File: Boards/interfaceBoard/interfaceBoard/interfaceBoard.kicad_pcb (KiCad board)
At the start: 2 copper layers, 100 x 100 mm, 49 parts, among them J1 Interface With Arduino, J2 12V input (molex), J3 Barrel_Jack_Switch, J4 MISO interface connector (Rea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, J5 Conn_02x09_Odd_Even, J6 DaisyCainOut, U1 74HC595, U2 TBD62783A, U3 74HC165, U4 74HC595, U5 TBD62783A, U6 74HC165

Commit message: Big progress
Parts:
- removed R10, R12, R14, R16, R18, R20, R22, R24, R26, R28, R30, R32, R34, R4, R6, R8: 100K, Resistor_THT:R_Axial_DIN0207_L6.3mm_D2.5mm_P10.16mm_Horizontal
- removed R11, R13, R15, R17, R19, R21, R23, R25, R27, R29, R31, R33, R5, R7, R9: 200K, Resistor_THT:R_Axial_DIN0207_L6.3mm_D2.5mm_P10.16mm_Horizontal
- added D3: LED, LED_THT:LED_D3.0mm, F.Cu at (68.4, 72.0)
- added RN1: R_Pack08, Package_DIP:DIP-16_W7.62mm_Socket, F.Cu at (90.0, 104.8)
- added RN2: R_Network08, Resistor_THT:R_Array_SIP9, F.Cu at (85.5, 102.3)
- added RN3: R_Pack08, Package_DIP:DIP-16_W7.62mm_Socket, F.Cu at (123.0, 105.4)
- added RN4: R_Network08, Resistor_THT:R_Array_SIP9, F.Cu at (118.5, 102.9)
- added RN5: R_Pack08, Package_DIP:DIP-16_W7.62mm_Socket, F.Cu at (91.1, 129.8)
- added RN6: R_Network08, Resistor_THT:R_Array_SIP9, F.Cu at (86.6, 127.2)
- added RN7: R_Pack08, Package_DIP:DIP-16_W7.62mm_Socket, F.Cu at (124.4, 130.1)
- added RN8: R_Network08, Resistor_THT:R_Array_SIP9, F.Cu at (119.9, 127.6)
- added SW1: SW_SPDT, myLibrary:SW_SPDT_SS-12D10L5, F.Cu at (71.5, 87.5)
- added U12: 74HC165, Package_DIP:DIP-16_W7.62mm_Socket, F.Cu at (104.4, 130.1)
- added U4: 74HC165, Package_DIP:DIP-16_W7.62mm_Socket, F.Cu at (103.0, 105.4)
- added U5: 74HC165, Package_DIP:DIP-16_W7.62mm_Socket, F.Cu at (71.1, 129.8)
- added U7: TBD62783A, Package_DIP:DIP-18_W7.62mm_Socket, F.Cu at (87.5, 76.9)
- added U8: 74HC595, Package_DIP:DIP-16_W7.62mm_Socket, F.Cu at (127.7, 76.8)
- added U9: TBD62783A, Package_DIP:DIP-18_W7.62mm_Socket, F.Cu at (116.0, 76.8)
- J4: value MISO interface connector (Read) -> Conn_02x17_Odd_Even; footprint Connector_PinHeader_2.54mm:PinHeader_2x09_P2.54mm_Vertical -> Connector_PinHeader_2.54mm:PinHeader_2x17_P2.54mm_Vertical
- J5: value Conn_02x09_Odd_Even -> Conn_02x17_Odd_Even; footprint Connector_PinHeader_2.54mm:PinHeader_2x09_P2.54mm_Vertical -> Connector_PinHeader_2.54mm:PinHeader_2x17_P2.54mm_Vertical
- R3: value 200K -> R
- U6: value 74HC165 -> 74HC595
- moved J4 67.4 mm to (145.0, 52.3)
- moved R3 59.9 mm to (82.1, 73.0)
- moved J5 51.5 mm to (145.0, 105.3)
- moved U6 44.8 mm to (99.2, 76.9)
- moved U3 24.2 mm to (70.0, 104.9)
- moved D2 14.5 mm to (68.4, 65.1)
- moved D1 14.4 mm to (68.4, 59.7)
- moved R2 13.0 mm to (82.1, 61.0)
- moved R1 12.9 mm to (82.1, 66.2)
- moved F1 10.2 mm to (77.5, 87.5), turned to 90 degrees
- moved U2 2.50 mm to (99.0, 51.9)
- moved J3 1.58 mm to (52.4, 55.0)
- moved U11 1.50 mm to (127.9, 51.8)
- moved J6 0.79 mm to (52.5, 148.0)
- renumbered J2 to J1, J3 to J2, J1 to J3, U4 to U10, U5 to U11
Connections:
- F1 pad 1: Net-(J2-Pin_2) -> Net-(SW1-B)
- J1 pad 2: Net-(J2-Pin_2) -> Net-(J1-Pin_2)
- J2 pad 1: Net-(J2-Pin_2) -> Net-(SW1-A)
- J4 pad 10: /MISO_sheet1/D0 -> /MOSI_sheet1/O1
- J4 pad 11: /MISO_sheet1/D1 -> /MOSI_sheet1/O2
- J4 pad 12: /MISO_sheet1/D2 -> /MOSI_sheet1/O3
- J4 pad 13: /MISO_sheet1/D3 -> /MOSI_sheet1/O4
- J4 pad 14: /MISO_sheet1/D4 -> /MOSI_sheet1/O5
- J4 pad 15: /MISO_sheet1/D5 -> /MOSI_sheet1/O6
- J4 pad 16: /MISO_sheet1/D6 -> /MOSI_sheet1/O7
- J4 pad 17: /MISO_sheet1/D7 -> /MOSI_sheet1/O8
- J4 pad 18: GND -> /MOSI_sheet2/O1
- J4 pad 2: /MISO_sheet/D0 -> /MOSI_sheet/O1
- J4 pad 3: /MISO_sheet/D1 -> /MOSI_sheet/O2
- J4 pad 4: /MISO_sheet/D2 -> /MOSI_sheet/O3
- J4 pad 5: /MISO_sheet/D3 -> /MOSI_sheet/O4
- J4 pad 6: /MISO_sheet/D4 -> /MOSI_sheet/O5
- J4 pad 7: /MISO_sheet/D5 -> /MOSI_sheet/O6
- J4 pad 8: /MISO_sheet/D6 -> /MOSI_sheet/O7
- J4 pad 9: /MISO_sheet/D7 -> /MOSI_sheet/O8
- J5 pad 10: /MOSI_sheet1/O1 -> /MISO_sheet1/D0
- J5 pad 11: /MOSI_sheet1/O2 -> /MISO_sheet1/D1
- J5 pad 12: /MOSI_sheet1/O3 -> /MISO_sheet1/D2
- J5 pad 13: /MOSI_sheet1/O4 -> /MISO_sheet1/D3
- J5 pad 14: /MOSI_sheet1/O5 -> /MISO_sheet1/D4
- J5 pad 15: /MOSI_sheet1/O6 -> /MISO_sheet1/D5
- J5 pad 16: /MOSI_sheet1/O7 -> /MISO_sheet1/D6
- J5 pad 17: /MOSI_sheet1/O8 -> /MISO_sheet1/D7
- J5 pad 18: GND -> /MISO_sheet2/D0
- J5 pad 2: /MOSI_sheet/O1 -> /MISO_sheet/D0
- J5 pad 3: /MOSI_sheet/O2 -> /MISO_sheet/D1
- J5 pad 4: /MOSI_sheet/O3 -> /MISO_sheet/D2
- J5 pad 5: /MOSI_sheet/O4 -> /MISO_sheet/D3
- J5 pad 6: /MOSI_sheet/O5 -> /MISO_sheet/D4
- J5 pad 7: /MOSI_sheet/O6 -> /MISO_sheet/D5
- J5 pad 8: /MOSI_sheet/O7 -> /MISO_sheet/D6
- J5 pad 9: /MOSI_sheet/O8 -> /MISO_sheet/D7
- J6 pad 3: /MOSI_sheet1/QH' -> /MOSI_sheet3/QH'
- J6 pad 4: /MISO_sheet1/SerIn -> /MISO_sheet3/SerIn
- R3 pad 1: /MISO_sheet/D1 -> 12V+
- R3 pad 2: /MISO_sheet/vDiv1/OUT -> Net-(D3-A)
- U3 pad 11: /MISO_sheet/vDiv0/OUT -> Net-(RN1-R8.1)
- U3 pad 12: /MISO_sheet/vDiv1/OUT -> Net-(RN1-R7.1)
- U3 pad 13: /MISO_sheet/vDiv2/OUT -> Net-(RN1-R6.1)
- U3 pad 14: /MISO_sheet/vDiv3/OUT -> Net-(RN1-R5.1)
- U3 pad 16: /MISO_sheet/5V+ -> 5V+
- U3 pad 3: /MISO_sheet/vDiv4/OUT -> Net-(RN1-R4.1)
- U3 pad 4: /MISO_sheet/vDiv5/OUT -> Net-(RN1-R3.1)
- U3 pad 5: /MISO_sheet/vDiv6/OUT -> Net-(RN1-R2.1)
- U3 pad 6: /MISO_sheet/vDiv7/OUT -> Net-(RN1-R1.1)
- U3 pad 9: /MISO_sheet/Q7 -> /MISO
- U6 pad 1: LOAD -> /MOSI_sheet2/QB
- U6 pad 10: /MISO_sheet1/SerIn -> 5V+
- U6 pad 11: /MISO_sheet1/vDiv0/OUT -> CLK
- U6 pad 12: /MISO_sheet1/vDiv1/OUT -> LATCH
- U6 pad 13: /MISO_sheet1/vDiv2/OUT -> GND
- U6 pad 14: /MISO_sheet1/vDiv3/OUT -> /MOSI_sheet1/QH'
- U6 pad 15: GND -> /MOSI_sheet2/QA
- U6 pad 16: /MISO_sheet1/5V+ -> 5V+
- U6 pad 2: CLK -> /MOSI_sheet2/QC
- U6 pad 3: /MISO_sheet1/vDiv4/OUT -> /MOSI_sheet2/QD
- U6 pad 4: /MISO_sheet1/vDiv5/OUT -> /MOSI_sheet2/QE
- U6 pad 5: /MISO_sheet1/vDiv6/OUT -> /MOSI_sheet2/QF
- U6 pad 6: /MISO_sheet1/vDiv7/OUT -> /MOSI_sheet2/QG
- U6 pad 7: unconnected-(U6-~{Q7}-Pad7) -> /MOSI_sheet2/QH
- U6 pad 9: /MISO_sheet/SerIn -> /MOSI_sheet2/QH'
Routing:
- net Net-(RN5-R1.1): track 0.00 -> 32.2 mm
- net Net-(RN3-R1.1): track 0.00 -> 32.2 mm
- net Net-(RN7-R1.1): track 0.00 -> 32.2 mm
- net Net-(RN1-R1.1): track 0.00 -> 32.2 mm
- net /MISO_sheet/vDiv3/OUT: track 26.5 -> 0.00 mm
- net /MISO_sheet1/vDiv3/OUT: track 26.5 -> 0.00 mm
- net /MISO_sheet/vDiv0/OUT: track 26.5 -> 0.00 mm
- net /MISO_sheet1/vDiv0/OUT: track 26.5 -> 0.00 mm
- net Net-(RN5-R4.1): track 0.00 -> 25.4 mm
- net Net-(RN1-R4.1): track 0.00 -> 25.4 mm
- net Net-(RN3-R4.1): track 0.00 -> 25.4 mm
- net Net-(RN7-R4.1): track 0.00 -> 25.4 mm
- net /MISO_sheet/vDiv1/OUT: track 24.4 -> 0.00 mm
- net /MISO_sheet1/vDiv1/OUT: track 24.4 -> 0.00 mm
- net /MISO_sheet/vDiv2/OUT: track 24.4 -> 0.00 mm
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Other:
- board text added: "ARDUINO STATUS LEDs"
- board text added: "BLUE: 12V+ POWER STATUS"
- board text added: "RED: STANDBY REG&GREEN: RUNNING GREEN: DONE SUCCESS! GREEN&RED BLINK: DONE FAIL"

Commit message: BEFORE FUCKING EVERYTHING UP
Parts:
- moved U8 19.4 mm to (123.2, 95.7), turned to 180 degrees
- moved U6 19.3 mm to (94.7, 95.7), turned to 180 degrees
- moved U9 12.1 mm to (128.1, 76.9)
- moved U7 12.1 mm to (99.6, 76.9)
- moved J3 7.55 mm to (59.8, 53.5), turned to -90 degrees
- moved RN4 1.73 mm to (119.8, 101.7)
- moved U4 1.73 mm to (104.3, 104.3)
- moved RN3 1.73 mm to (124.3, 104.3)
- moved U5 1.12 mm to (70.0, 130.1)
- moved RN5 1.12 mm to (90.0, 130.1)
- moved RN6 1.12 mm to (85.5, 127.6)
- moved U10 1.04 mm to (123.2, 70.5)
- moved U2 0.62 mm to (99.6, 51.8)
- moved U1 0.62 mm to (94.7, 70.5)
- moved RN1 0.58 mm to (90.0, 104.3)
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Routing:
- net 12V+: track 0.00 -> 118.7 mm
- net 5V+: track 0.00 -> 64.7 mm
- net /STATUS: track 0.00 -> 41.5 mm
- net Net-(D2-A): track 0.00 -> 16.7 mm
- net /MOSI_sheet2/QA: track 0.00 -> 14.9 mm
- net /MOSI_sheet1/QA: track 0.00 -> 14.9 mm
- net /MOSI_sheet/QA: track 0.00 -> 14.9 mm
- net /MOSI_sheet3/QA: track 0.00 -> 14.9 mm
- net /MOSI_sheet2/QG: track 0.00 -> 6.35 mm
- net /MOSI_sheet2/QF: track 0.00 -> 6.35 mm
- net /MOSI_sheet2/QD: track 0.00 -> 6.35 mm
- net /MOSI_sheet2/QB: track 0.00 -> 6.35 mm
- net /MOSI_sheet3/QH: track 0.00 -> 6.35 mm
- net /MOSI_sheet3/QF: track 0.00 -> 6.35 mm
- net /MOSI_sheet3/QD: track 0.00 -> 6.35 mm
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
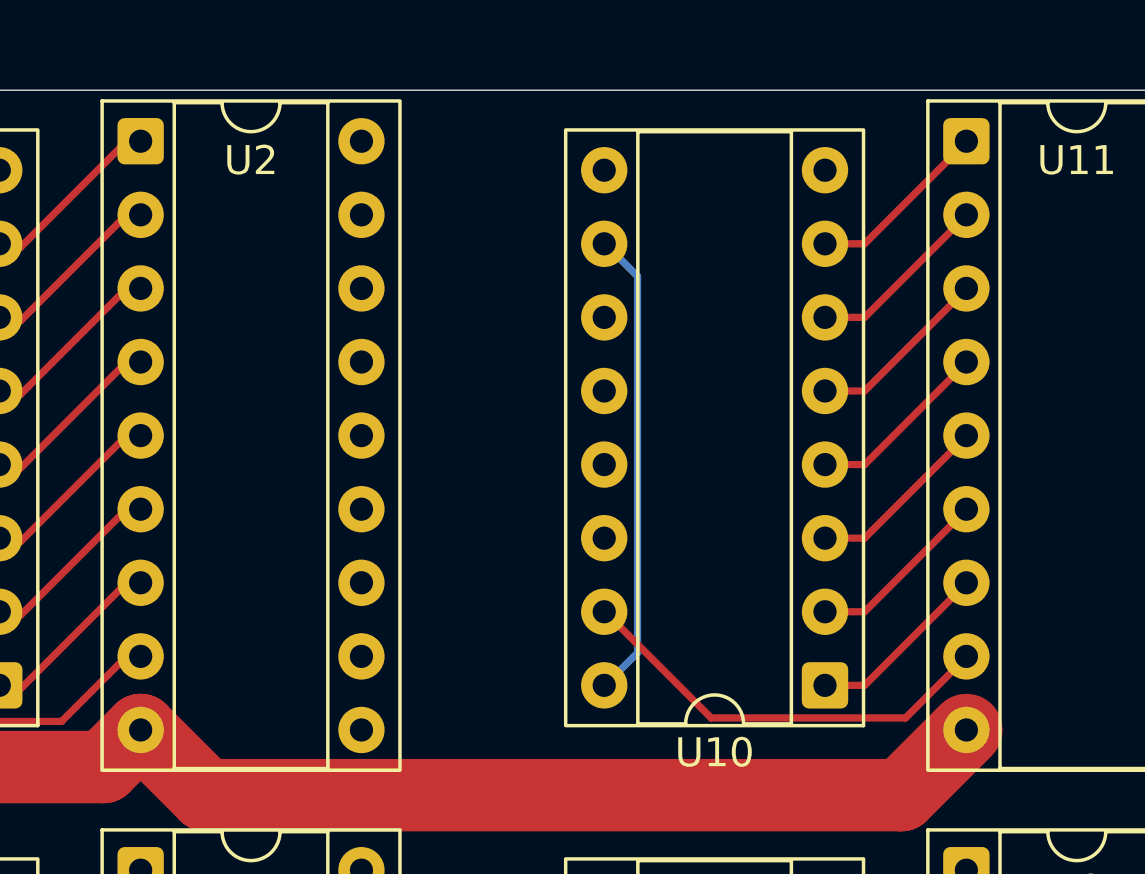
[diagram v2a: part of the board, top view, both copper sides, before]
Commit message: Update interfaceBoard.kicad_pcb
Started routing MOSI
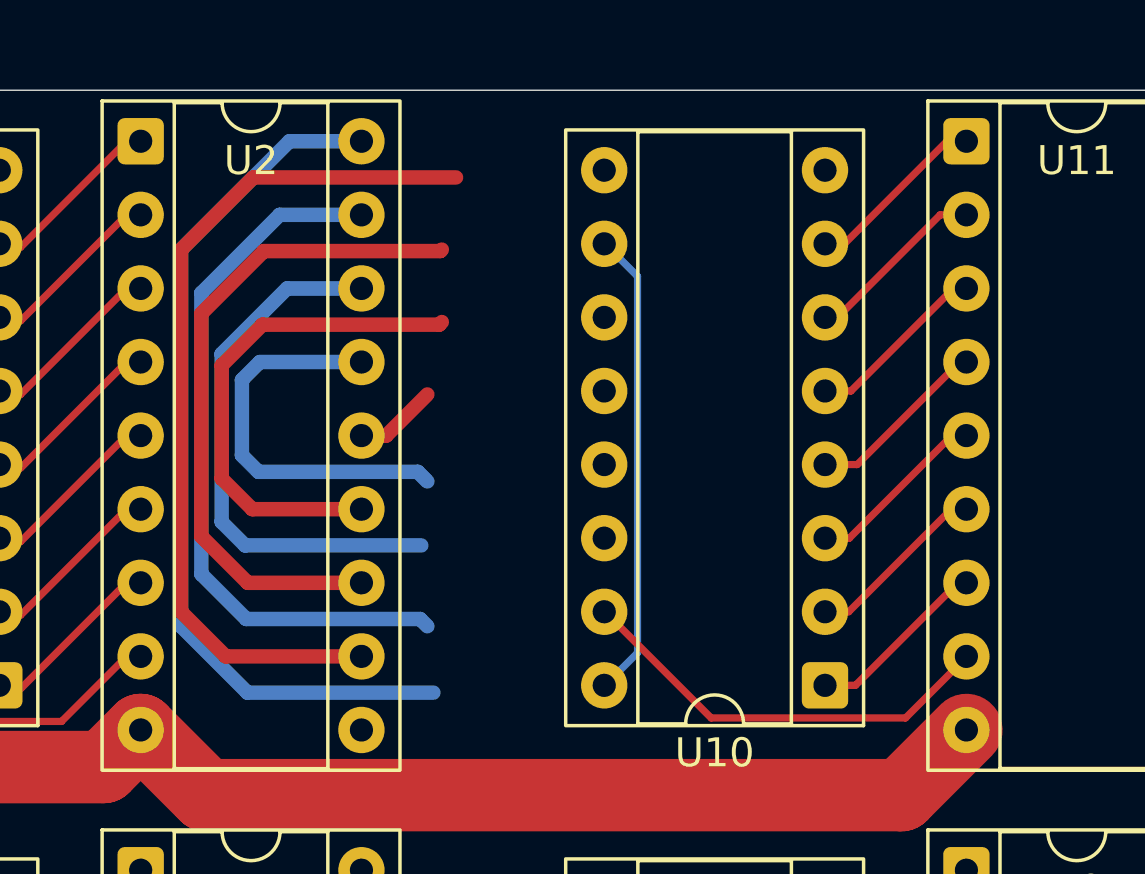
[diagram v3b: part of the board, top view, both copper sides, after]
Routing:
- net /MOSI_sheet/O8: track 0.00 -> 30.4 mm
- net /MOSI_sheet/O1: track 0.00 -> 29.9 mm
- net /MOSI_sheet/O7: track 0.00 -> 24.9 mm
- net /MOSI_sheet/O2: track 0.00 -> 23.1 mm
- net /MOSI_sheet/O6: track 0.00 -> 18.8 mm
- net /MOSI_sheet/O3: track 0.00 -> 17.4 mm
- net /MOSI_sheet/O5: track 0.00 -> 13.8 mm
- net /MOSI_sheet/O4: track 0.00 -> 2.86 mm

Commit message: Update interfaceBoard.kicad_pcb
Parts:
- moved J4 75.5 mm to (210.3, 90.3), turned to 180 degrees
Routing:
- net /MOSI_sheet/O8: track 30.4 -> 0.00 mm
- net /MOSI_sheet/O1: track 29.9 -> 0.00 mm
- net /MOSI_sheet/O7: track 24.9 -> 0.00 mm
- net /MOSI_sheet/O2: track 23.1 -> 0.00 mm
- net /MOSI_sheet/O6: track 18.8 -> 0.00 mm
- net /MOSI_sheet/O3: track 17.4 -> 0.00 mm
- net /MOSI_sheet/O5: track 13.8 -> 0.00 mm
- net /MOSI_sheet/O4: track 2.86 -> 0.00 mm

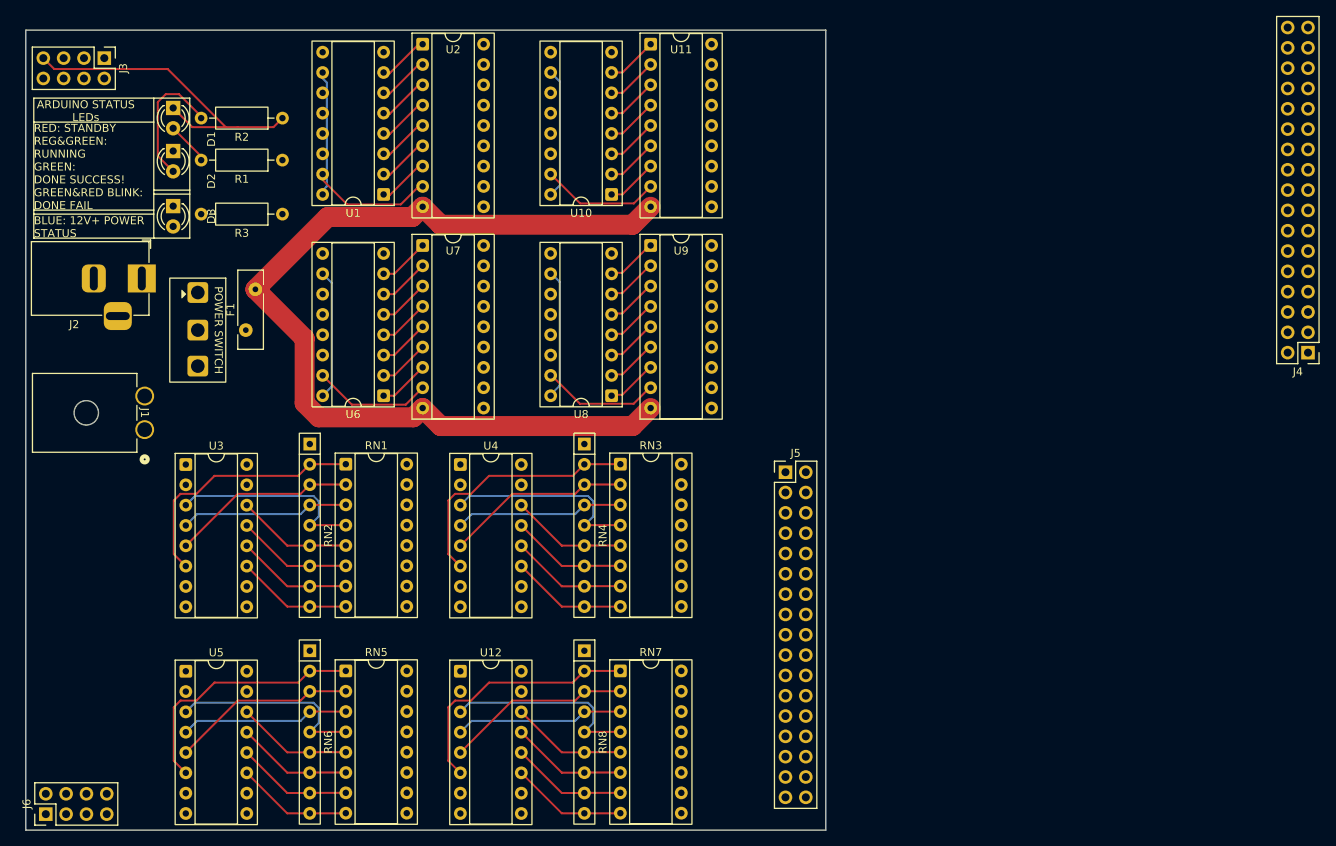
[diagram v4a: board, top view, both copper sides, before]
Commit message: WIP MOSI
Rearanged MOSI channels and wires MOSI0 and MOSI1 to output connector
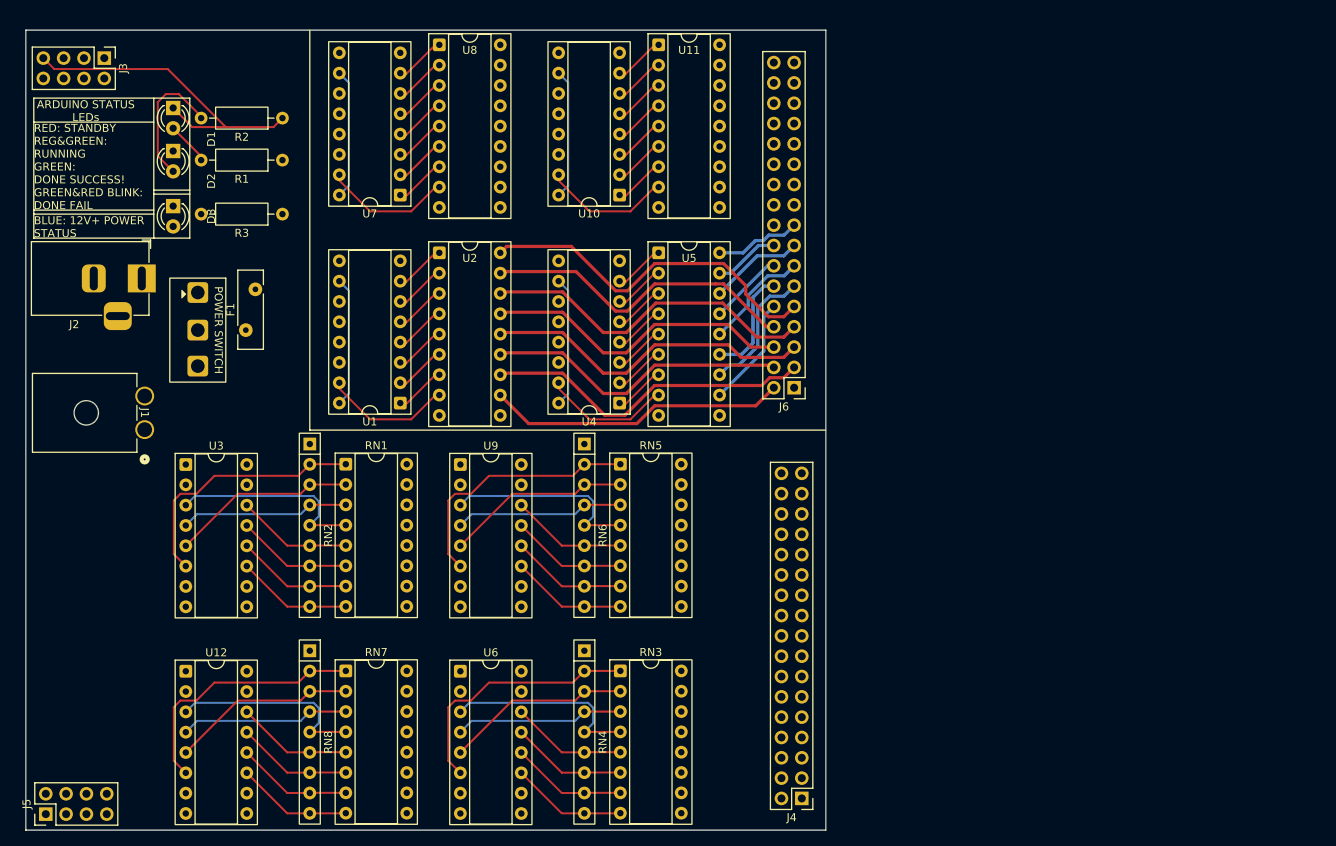
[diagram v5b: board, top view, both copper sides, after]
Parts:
- moved J6 64.4 mm to (146.0, 94.7)
- moved J4 40.8 mm to (147.0, 146.0), turned to 180 degrees
- moved U2 26.2 mm to (101.7, 77.8)
- moved U1 26.2 mm to (96.8, 96.6)
- moved U5 26.1 mm to (129.1, 77.8)
- moved U4 26.1 mm to (124.2, 96.6)
- moved U7 25.2 mm to (96.8, 70.6)
- moved U8 25.2 mm to (101.7, 51.8)
- moved U10 25.1 mm to (124.2, 70.6)
- moved U11 25.1 mm to (129.1, 51.8)
- renumbered J5 to J4, J6 to J5, J4 to J6, RN7 to RN3, RN8 to RN4, RN3 to RN5, RN4 to RN6, RN5 to RN7, RN6 to RN8, U8 to U10, U9 to U11, U5 to U12, U10 to U4, U11 to U5, U12 to U6, U6 to U7, U7 to U8, U4 to U9
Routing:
- net 12V+: track 118.7 -> 0.00 mm
- net /MOSI_sheet/O8: track 0.00 -> 44.7 mm
- net /MOSI_sheet/O6: track 0.00 -> 42.7 mm
- net /MOSI_sheet/O4: track 0.00 -> 41.6 mm
- net /MOSI_sheet/O2: track 0.00 -> 41.5 mm
- net /MOSI_sheet/O7: track 0.00 -> 39.9 mm
- net /MOSI_sheet/O5: track 0.00 -> 39.0 mm
- net /MOSI_sheet/O3: track 0.00 -> 38.0 mm
- net /MOSI_sheet/O1: track 0.00 -> 37.5 mm
- net /MOSI_sheet1/O2: track 0.00 -> 16.7 mm
- net /MOSI_sheet1/O1: track 0.00 -> 13.9 mm
- net /MOSI_sheet1/O3: track 0.00 -> 13.7 mm
- net /MOSI_sheet1/O4: track 0.00 -> 13.6 mm
- net /MOSI_sheet1/O6: track 0.00 -> 11.8 mm
- net /MOSI_sheet1/O8: track 0.00 -> 10.7 mm
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
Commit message: MOSI done?
MOSI wired.
MISO wired to interface
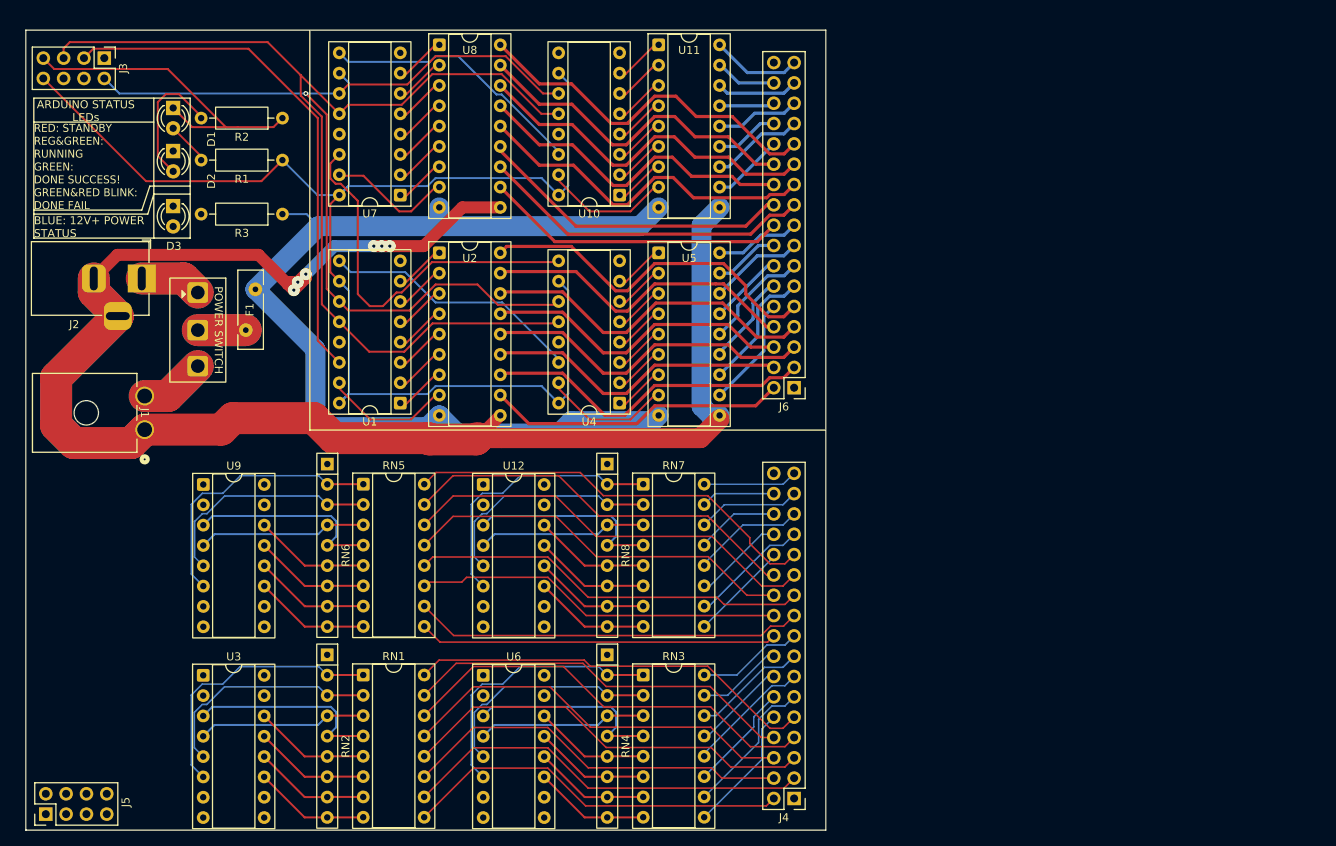
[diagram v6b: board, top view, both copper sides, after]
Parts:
- moved U12 43.9 mm to (107.2, 106.8)
- moved RN8 43.9 mm to (122.7, 104.2)
- moved RN7 43.9 mm to (127.2, 106.8)
- moved RN5 32.2 mm to (92.2, 106.8)
- moved RN6 32.2 mm to (87.7, 104.2)
- moved U9 32.2 mm to (72.2, 106.8)
- moved RN1 26.4 mm to (92.2, 130.6)
- moved RN2 26.4 mm to (87.7, 128.1)
- moved U3 26.4 mm to (72.2, 130.7)
- moved RN3 2.90 mm to (127.2, 130.6)
- moved RN4 2.90 mm to (122.7, 128.1)
- moved U6 2.90 mm to (107.2, 130.7)
- moved J4 0.96 mm to (146.0, 146.0)
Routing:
- net GND: track 0.00 -> 243.9 mm, vias 0 -> 6
- net LATCH: track 0.00 -> 134.6 mm
- net 12V+: track 0.00 -> 126.9 mm
- net CLK: track 0.00 -> 119.6 mm, vias 0 -> 1
- net 5V+: track 64.9 -> 180.2 mm
- net /MOSI: track 0.00 -> 65.0 mm
- net /MISO_sheet/D5: track 0.00 -> 53.4 mm
- net /MISO_sheet2/D5: track 0.00 -> 53.0 mm
- net /MISO_sheet2/D7: track 0.00 -> 52.5 mm
- net /MISO_sheet/D3: track 0.00 -> 52.4 mm
- net /MISO_sheet/D1: track 0.00 -> 51.4 mm
- net /MISO_sheet/D7: track 0.00 -> 51.1 mm
- net /MISO_sheet2/D6: track 0.00 -> 50.3 mm
- net /MISO_sheet/D4: track 0.00 -> 49.9 mm
- net /MISO_sheet2/D3: track 0.00 -> 49.6 mm
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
